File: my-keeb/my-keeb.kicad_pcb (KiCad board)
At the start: 2 copper layers, 190.5 x 95.2 mm, 108 parts, among them SW1 SW_Push, U1 ATmega32U4-AU, Y1 16MHz

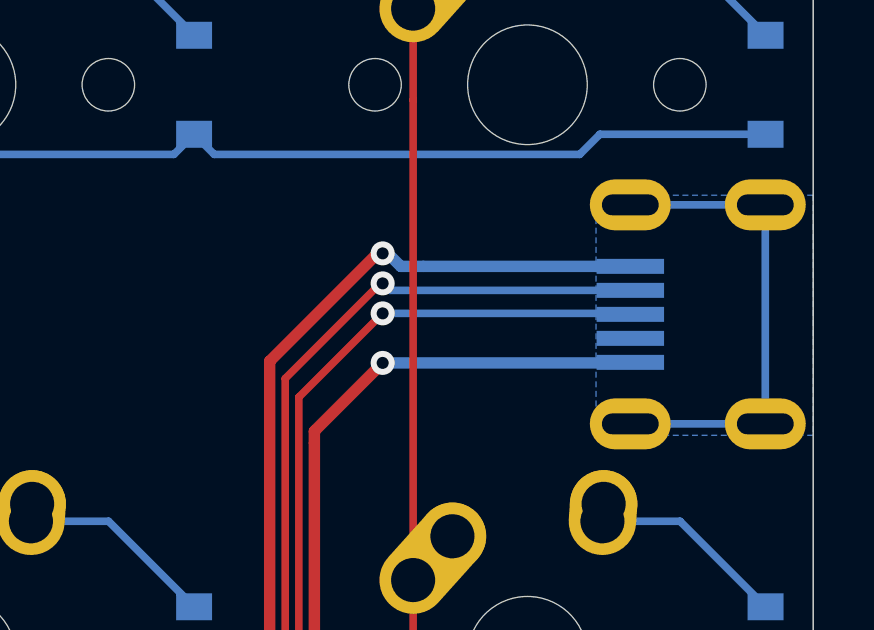
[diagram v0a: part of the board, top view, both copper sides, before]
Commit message: Updated my-keeb pcb
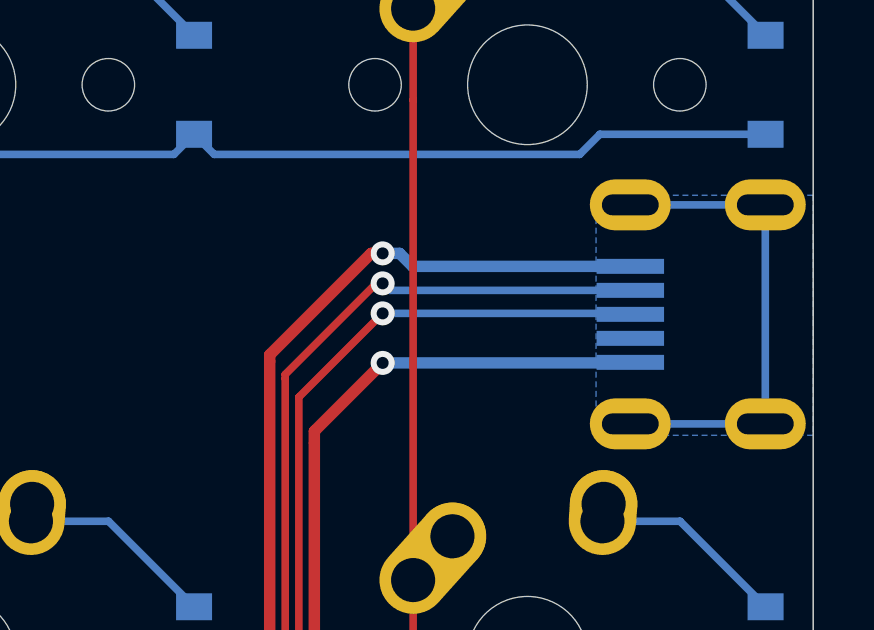
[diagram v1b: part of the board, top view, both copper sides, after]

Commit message: Improved USB routing for original my-keeb
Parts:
- moved USB1 95.9 mm to (108.0, 9.27), turned to 270 degrees
- moved D19 11.2 mm to (98.4, 30.2), turned to 0 degrees
- moved C6 3.31 mm to (191.9, 87.6), turned to 90 degrees
- moved R1 2.73 mm to (186.6, 88.7)
- moved R2 2.48 mm to (188.7, 88.7)
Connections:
- net Net-(R1-Pad1) renamed DN
- net Net-(R2-Pad1) renamed DP
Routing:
- net GND: track 144.9 -> 229.9 mm, vias 2 -> 0
- net D+: track 67.4 -> 149.0 mm, vias 2 -> 0
- net VCC: track 72.6 -> 153.6 mm, vias 2 -> 0
- net D-: track 69.4 -> 149.0 mm, vias 2 -> 0
- net Net-(D19-Pad2): track 6.62 -> 12.8 mm
- net ROW0: track 259.5 -> 265.3 mm, vias 2 -> 4
- net Net-(C6-Pad1): track 3.26 -> 5.50 mm
- net DN: track 5.22 -> 3.13 mm
- net +5V: track 110.1 -> 111.4 mm, vias 0 -> 2
- net DP: track 3.71 -> 3.14 mm
- net ROW2: track 223.5 -> 223.8 mm, vias 2 -> 4
- net ROW3: track 205.6 -> 205.9 mm, vias 0 -> 2
- net ROW1: track 241.5 -> 241.7 mm, vias 2 -> 4
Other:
- board size 190.5 x 95.2 mm -> 190.5 x 100.3 mm
